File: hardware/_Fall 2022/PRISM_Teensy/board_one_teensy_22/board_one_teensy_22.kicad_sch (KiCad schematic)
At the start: 15 parts, among them J1 Conn_01x04, J2 Conn_01x07, U1 Teensy4.1, U2 BNO055_Breakout, U3 BMP388

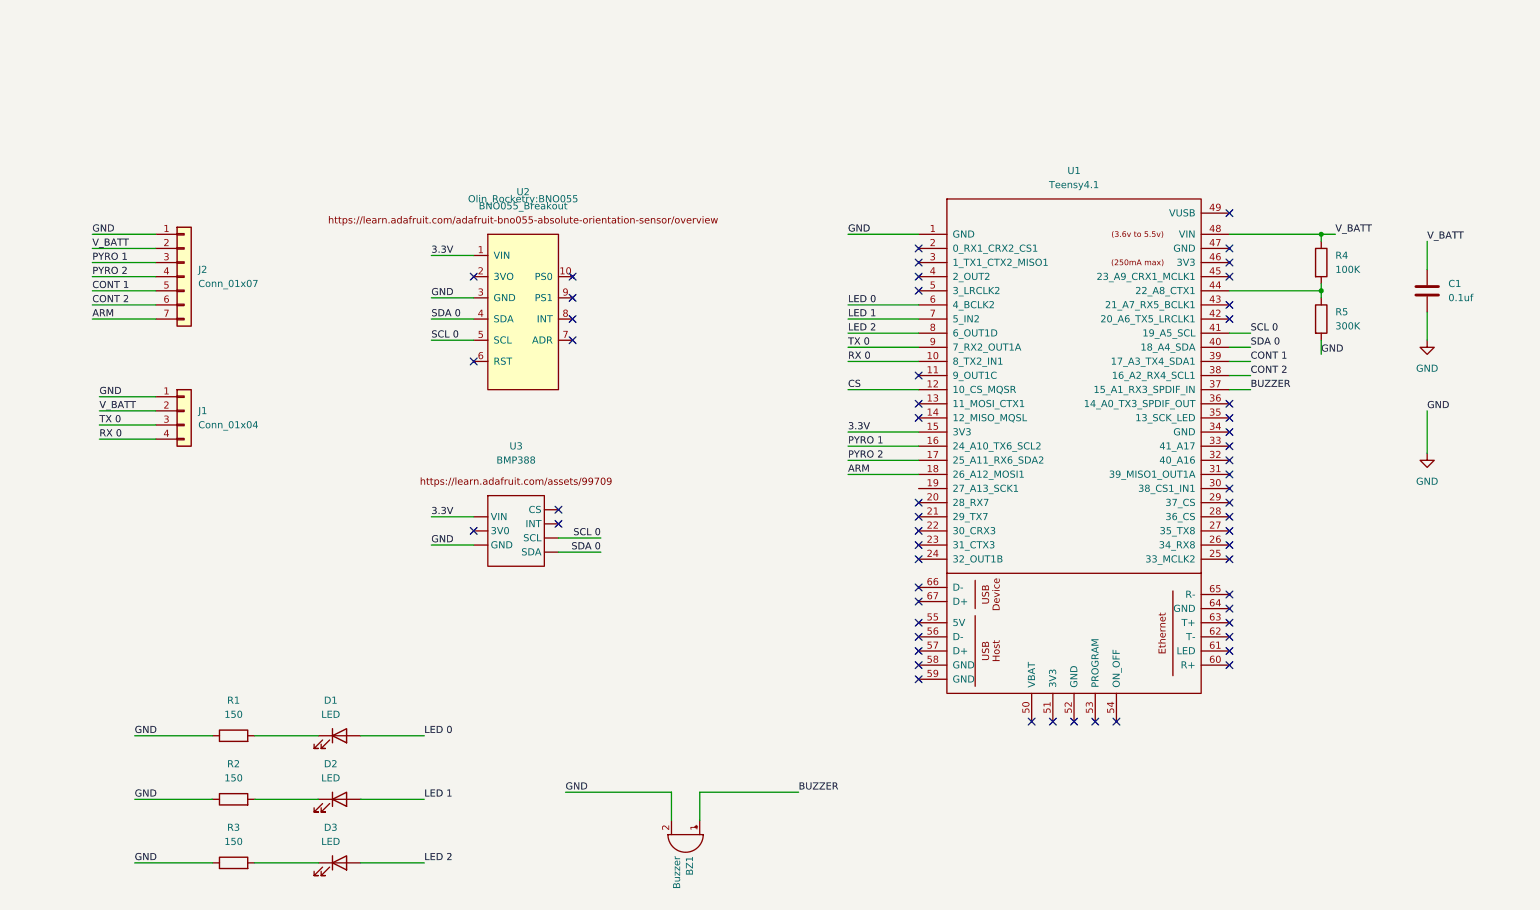
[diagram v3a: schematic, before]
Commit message: reorganized PRISM FC
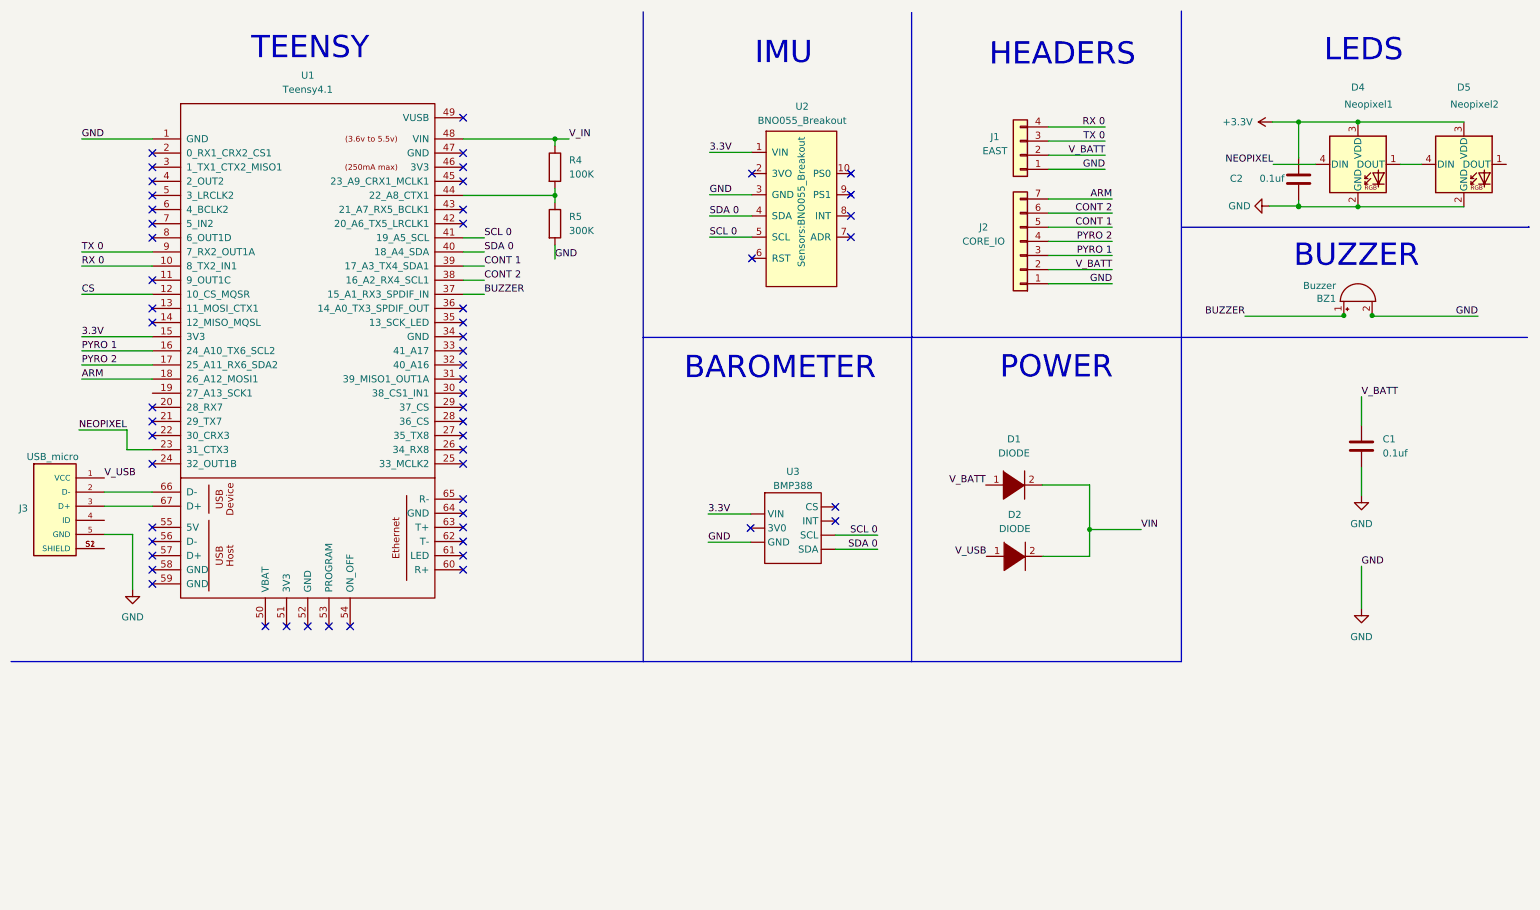
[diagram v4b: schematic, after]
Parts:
- removed D1, D2, D3: LED, LED_SMD:LED_0805_2012Metric_Pad1.15x1.40mm_HandSolder, symbol Device:LED
- removed R1, R2, R3: 150, Resistor_SMD:R_0805_2012Metric_Pad1.20x1.40mm_HandSolder, symbol Device:R
- added C2: 0.1uf, Capacitor_Tantalum_SMD:CP_EIA-1608-08_AVX-J, symbol Device:C
- added D1, D2: DIODE, Diode_SMD:D_0201_0603Metric, symbol pspice:DIODE
- added D4: Neopixel1, neopixel:LED_1655, symbol LED:NeoPixel_THT
- added D5: Neopixel2, neopixel:LED_1655, symbol LED:NeoPixel_THT
- added J3: USB_micro, USB:GCT_USB3131-30-0230-A_REVB, symbol USB:USB3131-30-0230-A_REVB
- J1: value Conn_01x04 -> EAST
- J2: value Conn_01x07 -> CORE_IO
- U2: footprint Olin_Rocketry:BNO055 -> Sensors:BNO055_Breakout
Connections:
- net GND: now also C2.1, D4.2 (GND), D5.2 (GND), J3.5 (GND)
- net V_BATT: now also D1.1 (K); no longer R4.1, U1.48 (VIN)
- net NEOPIXEL: now reaches U1.23 (31_CTX3)
- net NEOPIXEL: now also D4.4 (DIN)
- net at U1.66 (D-): now also J3.2 (D-)
- net at U1.67 (D+): now also J3.3 (D+)
- net LED 0: no longer names the net of U1.6 (4_BCLK2)
- net LED 1: no longer names the net of U1.7 (5_IN2)
- net LED 2: no longer names the net of U1.8 (6_OUT1D)
- new net: D4.1 (DOUT), D5.4 (DIN)
- new net: J3.S1 (SHIELD), J3.S2 (SHIELD)
- new net +3.3V: C2.2, D4.3 (VDD), D5.3 (VDD)
- new net VIN: D1.2 (A), D2.2 (A)
- new net V_IN: R4.1, U1.48 (VIN)
- new net V_USB: D2.1 (K), J3.1 (VCC)
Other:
- note added: "BAROMETER"
- note added: "BUZZER"
- note added: "HEADERS"
- note added: "IMU"
- note added: "LEDS"
- note added: "POWER"
- note added: "TEENSY"
- moved on the sheet: BZ1, C1, J1, J2, R4, R5, U1

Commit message: work on PRISM io
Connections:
- net ARM: now also J2.1 (Pin_1); no longer J2.7 (Pin_7)
- net CONT 1: now also J2.3 (Pin_3); no longer J2.5 (Pin_5)
- net CONT 2: now also J2.2 (Pin_2); no longer J2.6 (Pin_6)
- net GND: now also J2.7 (Pin_7); no longer J2.1 (Pin_1)
- net PYRO 1: now also J2.5 (Pin_5); no longer J2.3 (Pin_3)
- net V_BATT: no longer J2.2 (Pin_2)
- new net VBAT: J2.6 (Pin_6)
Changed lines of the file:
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@@
     (effects (font (size 1.27 1.27)) (justify left bottom))
   )
-  (label "GND" (at 210.058 60.96 180)
+  (label "ARM" (at 210.058 60.96 180)
     (effects (font (size 1.27 1.27)) (justify right bottom))
   )
@@
     (effects (font (size 1.27 1.27)) (justify left bottom))
   )
-  (label "V_BATT" (at 210.058 58.42 180)
+  (label "CONT 2" (at 210.058 58.42 180)
     (effects (font (size 1.27 1.27)) (justify right bottom))
   )
@@
     (effects (font (size 1.27 1.27)) (justify left bottom))
   )
-  (label "ARM" (at 210.058 45.72 180)
+  (label "GND" (at 210.058 45.72 180)
     (effects (font (size 1.27 1.27)) (justify right bottom))
   )
@@
     (effects (font (size 1.27 1.27)) (justify left bottom))
   )
-  (label "CONT 2" (at 210.058 48.26 180)
+  (label "VBAT" (at 210.058 48.26 180)
     (effects (font (size 1.27 1.27)) (justify right bottom))
   )
@@
     (effects (font (size 1.27 1.27)) (justify left bottom))
   )
-  (label "CONT 1" (at 210.058 50.8 180)
+  (label "PYRO 1" (at 210.058 50.8 180)
     (effects (font (size 1.27 1.27)) (justify right bottom))
   )
@@
     (effects (font (size 1.27 1.27)) (justify left bottom))
   )
-  (label "PYRO 1" (at 210.058 55.88 180)
+  (label "CONT 1" (at 210.058 55.88 180)
     (effects (font (size 1.27 1.27)) (justify right bottom))
   )

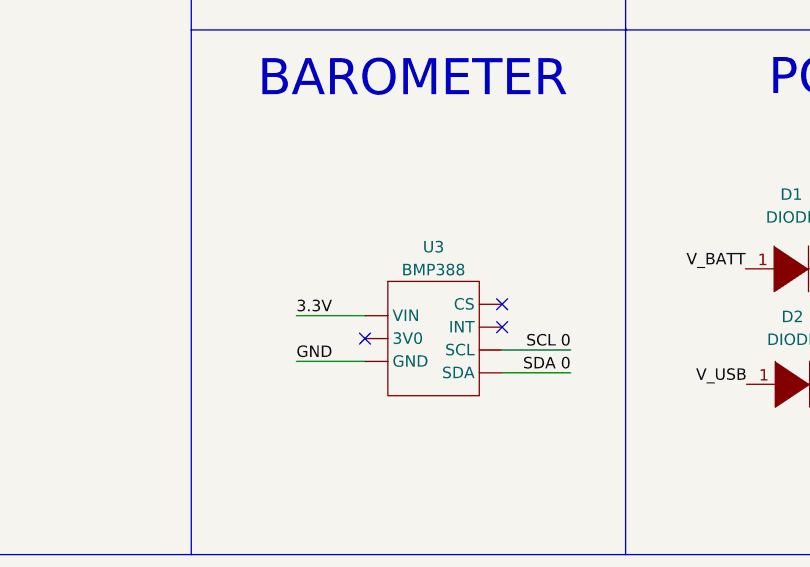
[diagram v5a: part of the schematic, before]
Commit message: Add altimeter files
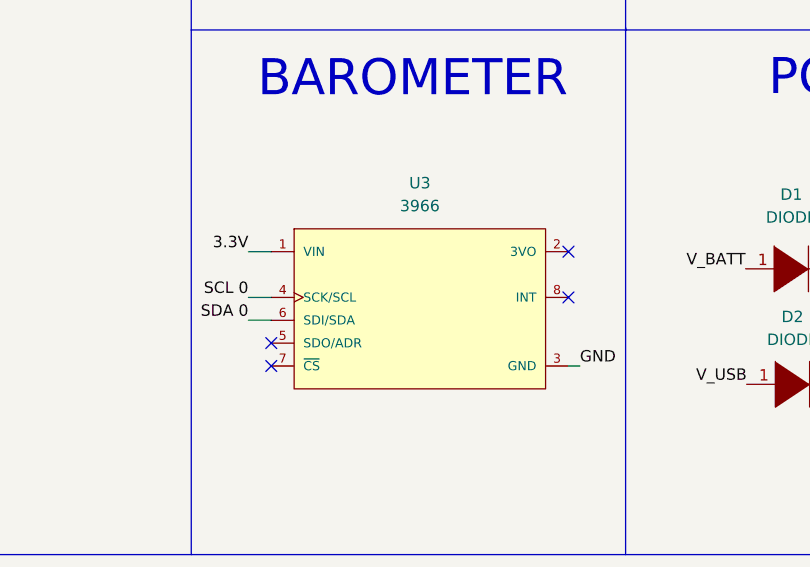
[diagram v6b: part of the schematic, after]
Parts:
- removed U3: BMP388, symbol Sensor:BMP3xx
- added U3: 3966, BMP388:Adafruit_Industries-3966-MFG, symbol BMP388:3966
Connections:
- net 3.3V: now also U3.1 (VIN)
- net GND: now also U3.3 (GND)
- net SCL 0: now also U3.4 (SCK/SCL)
- net SDA 0: now also U3.6 (SDI/SDA)
- no-connect marks 57 -> 58
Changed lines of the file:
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@@
   (junction (at 243.586 31.877) (diameter 0) (color 0 0 0 0)
   )
-  (no_connect (at 160.274 103.632))
-  (no_connect (at 160.274 101.092))
-  (no_connect (at 145.034 104.902))
   (no_connect (at 163.068 44.958))
   (no_connect (at 93.345 42.545))
@@
   (no_connect (at 163.068 48.768))
   (no_connect (at 145.288 41.148))
+  (no_connect (at 167.64 95.25))
+  (no_connect (at 167.64 100.33))
+  (no_connect (at 134.62 105.41))
+  (no_connect (at 134.62 107.95))
   (no_connect (at 37.465 52.705))
   (no_connect (at 37.465 50.165))
@@
     (stroke (width 0) (type default) (color 0 0 0 0))
   )
-  (wire (pts (xy 167.894 106.172) (xy 160.274 106.172))
-    (stroke (width 0) (type default) (color 0 0 0 0))
-  )
   (wire (pts (xy 210.058 55.88) (xy 198.628 55.88))
     (stroke (width 0) (type default) (color 0 0 0 0))
@@
     (stroke (width 0) (type default) (color 0 0 0 0))
   )
+  (wire (pts (xy 132.08 100.33) (xy 134.62 100.33))
+    (stroke (width 0) (type default) (color 0 0 0 0))
+  )
   (wire (pts (xy 243.586 31.877) (xy 243.586 38.354))
     (stroke (width 0) (type default) (color 0 0 0 0))
@@
     (stroke (width 0) (type default) (color 0 0 0 0))
   )
+  (wire (pts (xy 167.64 107.95) (xy 168.91 107.95))
+    (stroke (width 0) (type default) (color 0 0 0 0))
+  )
   (wire (pts (xy 145.288 37.338) (xy 137.668 37.338))
     (stroke (width 0) (type default) (color 0 0 0 0))
@@
     (stroke (width 0) (type default) (color 0 0 0 0))
   )
-  (wire (pts (xy 160.274 108.712) (xy 167.894 108.712))
-    (stroke (width 0) (type default) (color 0 0 0 0))
-  )
   (wire (pts (xy 24.765 62.865) (xy 37.465 62.865))
     (stroke (width 0) (type default) (color 0 0 0 0))
@@
     (stroke (width 0) (type default) (color 0 0 0 0))
   )
+  (wire (pts (xy 132.08 95.25) (xy 134.62 95.25))
+    (stroke (width 0) (type default) (color 0 0 0 0))
+  )
   (wire (pts (xy 197.612 109.982) (xy 205.994 109.982))
     (stroke (width 0) (type default) (color 0 0 0 0))
@@
     (stroke (width 0) (type default) (color 0 0 0 0))
   )
+  (wire (pts (xy 132.08 102.87) (xy 134.62 102.87))
+    (stroke (width 0) (type default) (color 0 0 0 0))
+  )
   (wire (pts (xy 208.788 35.306) (xy 198.628 35.306))
     (stroke (width 0) (type default) (color 0 0 0 0))
@@
     (stroke (width 0) (type default) (color 0 0 0 0))
   )
-  (wire (pts (xy 145.034 107.442) (xy 137.414 107.442))
-    (stroke (width 0) (type default) (color 0 0 0 0))
-  )
   (wire (pts (xy 243.586 46.99) (xy 243.586 47.117))
     (stroke (width 0) (type default) (color 0 0 0 0))
@@
   )
   (wire (pts (xy 251.714 66.802) (xy 233.934 66.802))
-    (stroke (width 0) (type default) (color 0 0 0 0))
-  )
-  (wire (pts (xy 137.414 102.362) (xy 145.034 102.362))
     (stroke (width 0) (type default) (color 0 0 0 0))
   )
@@
     (effects (font (size 1.27 1.27)) (justify left bottom))
   )
+  (label "3.3V" (at 132.08 95.25 180)
+    (effects (font (size 1.27 1.27)) (justify right bottom))
+  )
   (label "BUZZER" (at 97.155 62.865 0)
     (effects (font (size 1.27 1.27)) (justify left bottom))
   )
+  (label "SCL 0" (at 132.08 100.33 180)
+    (effects (font (size 1.27 1.27)) (justify right bottom))
+  )
   (label "CONT 2" (at 97.155 60.325 0)
     (effects (font (size 1.27 1.27)) (justify left bottom))
@@
     (effects (font (size 1.27 1.27)) (justify right bottom))
   )
-  (label "GND" (at 137.414 107.442 0)
-    (effects (font (size 1.27 1.27)) (justify left bottom))
-  )
   (label "SCL 0" (at 97.155 52.705 0)
     (effects (font (size 1.27 1.27)) (justify left bottom))
@@
     (effects (font (size 1.27 1.27)) (justify left bottom))
   )
+  (label "SDA 0" (at 132.08 102.87 180)
+    (effects (font (size 1.27 1.27)) (justify right bottom))
+  )
   (label "GND" (at 210.058 45.72 180)
     (effects (font (size 1.27 1.27)) (justify right bottom))
@@
     (effects (font (size 1.27 1.27)) (justify left bottom))
   )
-  (label "SDA 0" (at 167.894 108.712 180)
-    (effects (font (size 1.27 1.27)) (justify right bottom))
-  )
   (label "TX 0" (at 24.765 55.245 0)
     (effects (font (size 1.27 1.27)) (justify left bottom))
@@
     (effects (font (size 1.27 1.27)) (justify left bottom))
   )
-  (label "3.3V" (at 137.414 102.362 0)
-    (effects (font (size 1.27 1.27)) (justify left bottom))
-  )
   (label "RX 0 " (at 208.788 32.766 180)
     (effects (font (size 1.27 1.27)) (justify right bottom))
@@
     (effects (font (size 1.27 1.27)) (justify right bottom))
   )
+  (label "GND" (at 168.91 107.95 0)
+    (effects (font (size 1.27 1.27)) (justify left bottom))
+  )
   (label "CS" (at 24.765 62.865 0)
     (effects (font (size 1.27 1.27)) (justify left bottom))
@@
   )
   (label "PYRO 1" (at 210.058 50.8 180)
-    (effects (font (size 1.27 1.27)) (justify right bottom))
-  )
-  (label "SCL 0" (at 167.894 106.172 180)
     (effects (font (size 1.27 1.27)) (justify right bottom))
   )
@@
     (pin "4")
   )
+  (symbol (lib_id "BMP388:3966") (at 132.08 95.25 0) (unit 1)
+    (in_bom yes) (on_board yes) (fields_autoplaced)
+    (property "Reference" "U3" (id 0) (at 151.13 87.63 0))
+    (property "Value" "3966" (id 1) (at 151.13 90.17 0))
+    (property "Footprint" "BMP388:Adafruit_Industries-3966-MFG" (id 2) (at 132.08 85.09 0)
+      (effects (font (size 1.27 1.27)) (justify left) hide)
+    )
+    (property "Datasheet" "https://cdn-learn.adafruit.com/downloads/pdf/adafruit-bmp388-bmp390-bmp3xx.pdf?timestamp=1628517945" (id 3) (at 132.08 82.55 0)
+      (effects (font (size 1.27 1.27)) (justify left) hide)
+    )
+    (property "automotive" "No" (id 4) (at 132.08 80.01 0)
+      (effects (font (size 1.27 1.27)) (justify left) hide)
+    )
+    (property "category" "UNK" (id 5) (at 132.08 77.47 0)
+      (effects (font (size 1.27 1.27)) (justify left) hide)
+    )
+    (property "device class L1" "Sensors" (id 6) (at 132.08 74.93 0)
+      (effects (font (size 1.27 1.27)) (justify left) hide)
+    )
+    (property "device class L2" "Pressure Sensors" (id 7) (at 132.08 72.39 0)
+      (effects (font (size 1.27 1.27)) (justify left) hide)
+    )
+    (property "device class L3" "unset" (id 8) (at 132.08 69.85 0)
+      (effects (font (size 1.27 1.27)) (justify left) hide)
+    )
+    (property "digikey description" "BMP388 - PRECISION BAROMETRIC PR" (id 9) (at 132.08 67.31 0)
+      (effects (font (size 1.27 1.27)) (justify left) hide)
+    )
+    (property "digikey part number" "1528-2733-ND" (id 10) (at 132.08 64.77 0)
+      (effects (font (size 1.27 1.27)) (justify left) hide)
+    )
+    (property "lead free" "Yes" (id 11) (at 132.08 62.23 0)
+      (effects (font (size 1.27 1.27)) (justify left) hide)
+    )
+    (property "library id" "4429725cd9347a7a" (id 12) (at 132.08 59.69 0)
+      (effects (font (size 1.27 1.27)) (justify left) hide)
+    )
+    (property "manufacturer" "Adafruit Industries" (id 13) (at 132.08 57.15 0)
+      (effects (font (size 1.27 1.27)) (justify left) hide)
+    )
+    (property "mouser part number" "485-3966" (id 14) (at 132.08 54.61 0)
+      (effects (font (size 1.27 1.27)) (justify left) hide)
+    )
+    (property "package" "MODULE_25MM40_17MM78" (id 15) (at 132.08 52.07 0)
+      (effects (font (size 1.27 1.27)) (justify left) hide)
+    )
+    (property "rohs" "Yes" (id 16) (at 132.08 49.53 0)
+      (effects (font (size 1.27 1.27)) (justify left) hide)
+    )
+    (property "sensor output" "I2C,SPI" (id 17) (at 132.08 46.99 0)
+      (effects (font (size 1.27 1.27)) (justify left) hide)
+    )
+    (pin "1")
+    (pin "2")
+    (pin "3")
+    (pin "4")
+    (pin "5")
+    (pin "6")
+    (pin "7")
+    (pin "8")
+  )
   (symbol (lib_id "Device:R") (at 109.855 50.165 0) (unit 1)
     (in_bom yes) (on_board yes) (fields_autoplaced)
@@
     )
     (pin "1")
-  )
-  (symbol (lib_id "Sensor:BMP3xx") (at 152.654 108.712 0) (unit 1)
-    (in_bom yes) (on_board yes) (fields_autoplaced)
-    (property "Reference" "U3" (id 0) (at 152.654 94.742 0))
-    (property "Value" "BMP388" (id 1) (at 152.654 97.282 0))
-    (property "Footprint" "" (id 2) (at 151.384 108.712 0)
-      (effects (font (size 1.27 1.27)) hide)
-    )
-    (property "Datasheet" "" (id 3) (at 151.384 108.712 0)
-      (effects (font (size 1.27 1.27)) hide)
-    )
-    (pin "")
-    (pin "")
-    (pin "")
-    (pin "")
-    (pin "")
-    (pin "")
-    (pin "")
   )
   (symbol (lib_id "power:GND") (at 238.252 46.99 270) (unit 1)
@@
       (reference "U2") (unit 1) (value "BNO055_Breakout") (footprint "Sensors:BNO055_Breakout")
     )
-    (path "/ccabf454-515a-4eef-9f15-6a69b34f4a30"
-      (reference "U3") (unit 1) (value "BMP388") (footprint "")
-    )
-  )
+    (path "/a6652d03-f318-42dd-bed8-4ae28a7af164"
+      (reference "U3") (unit 1) (value "3966") (footprint "BMP388:Adafruit_Industries-3966-MFG")
+    )
+  )
